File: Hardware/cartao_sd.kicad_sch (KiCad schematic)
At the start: 2 parts, among them J17 Micro_SD_Card, U11 74LVC125

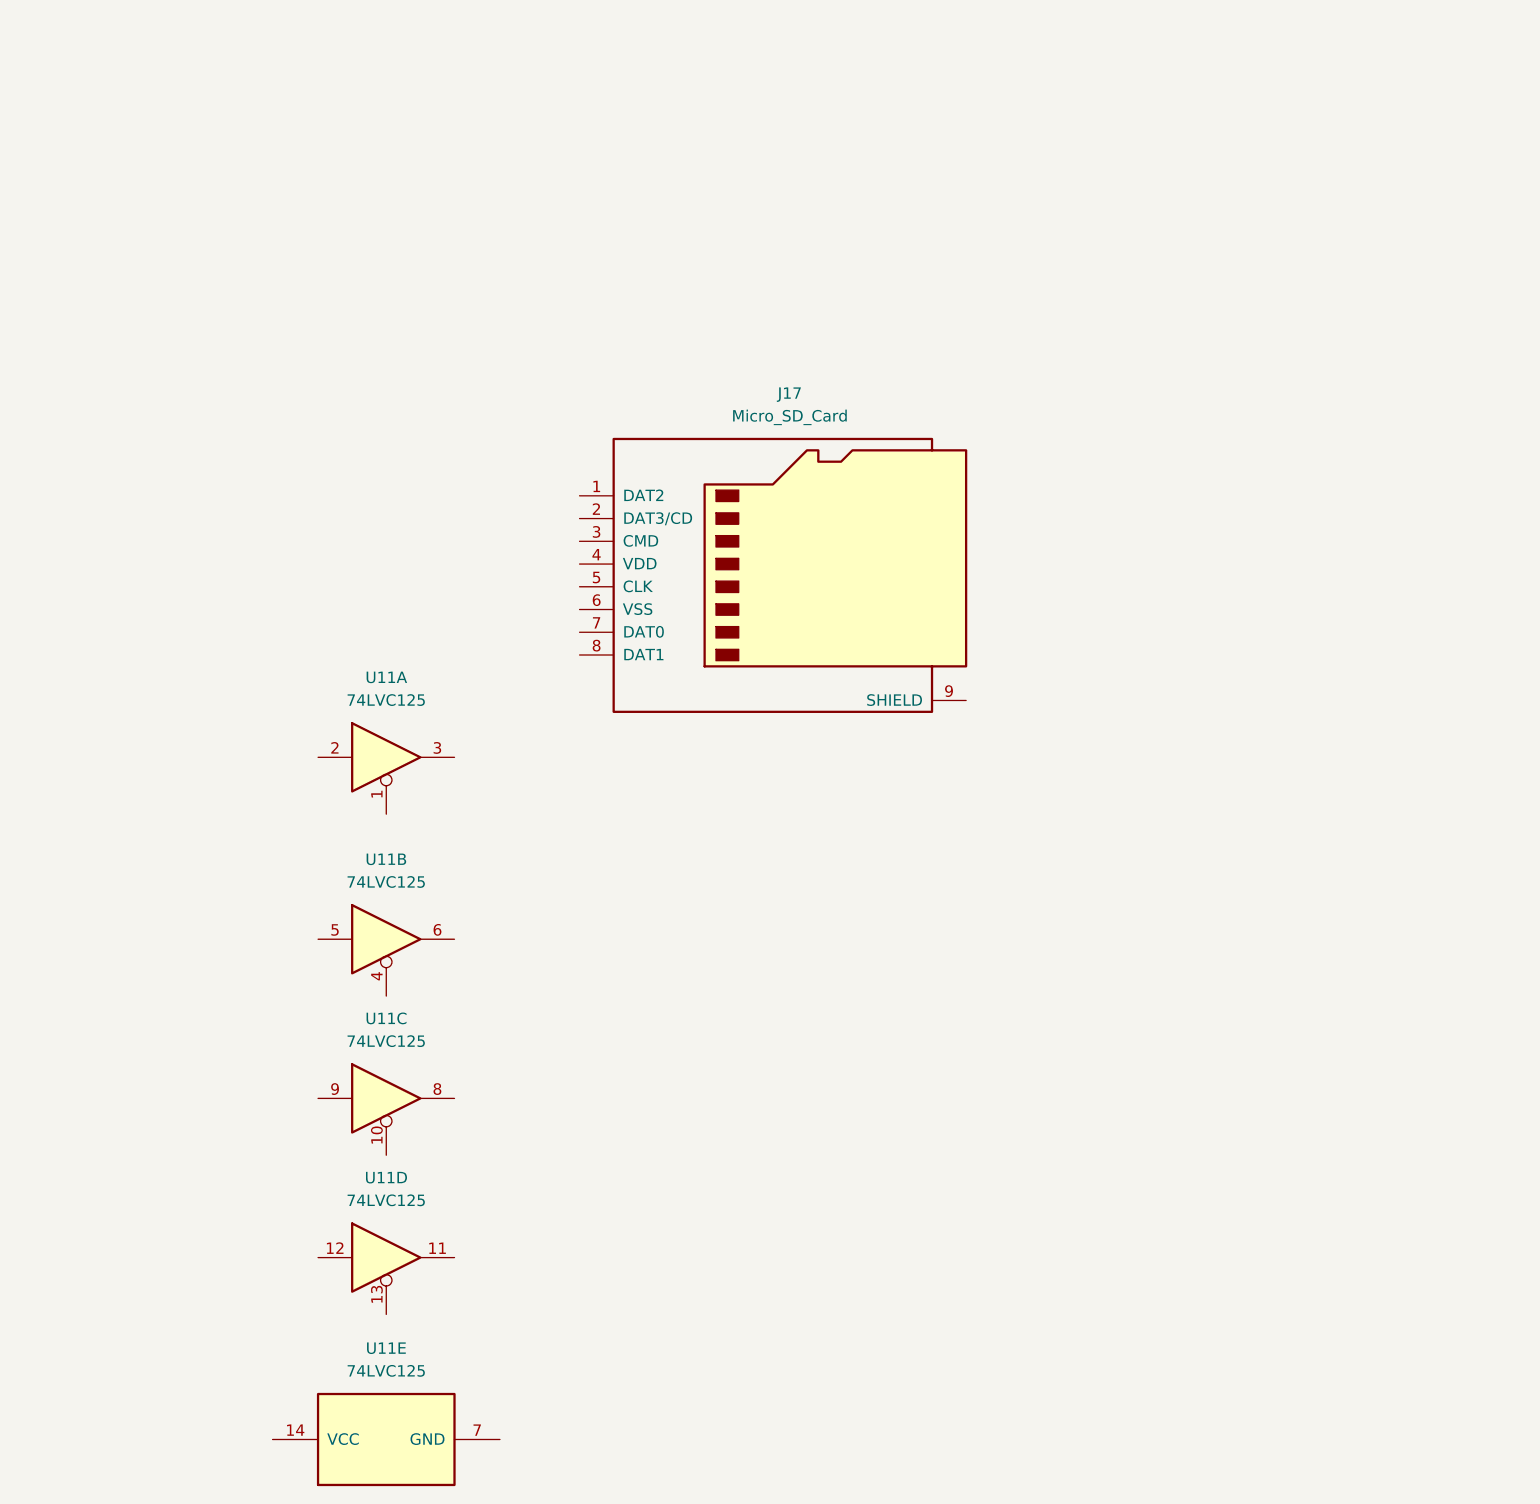
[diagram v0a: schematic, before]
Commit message: add circuito cartão sd
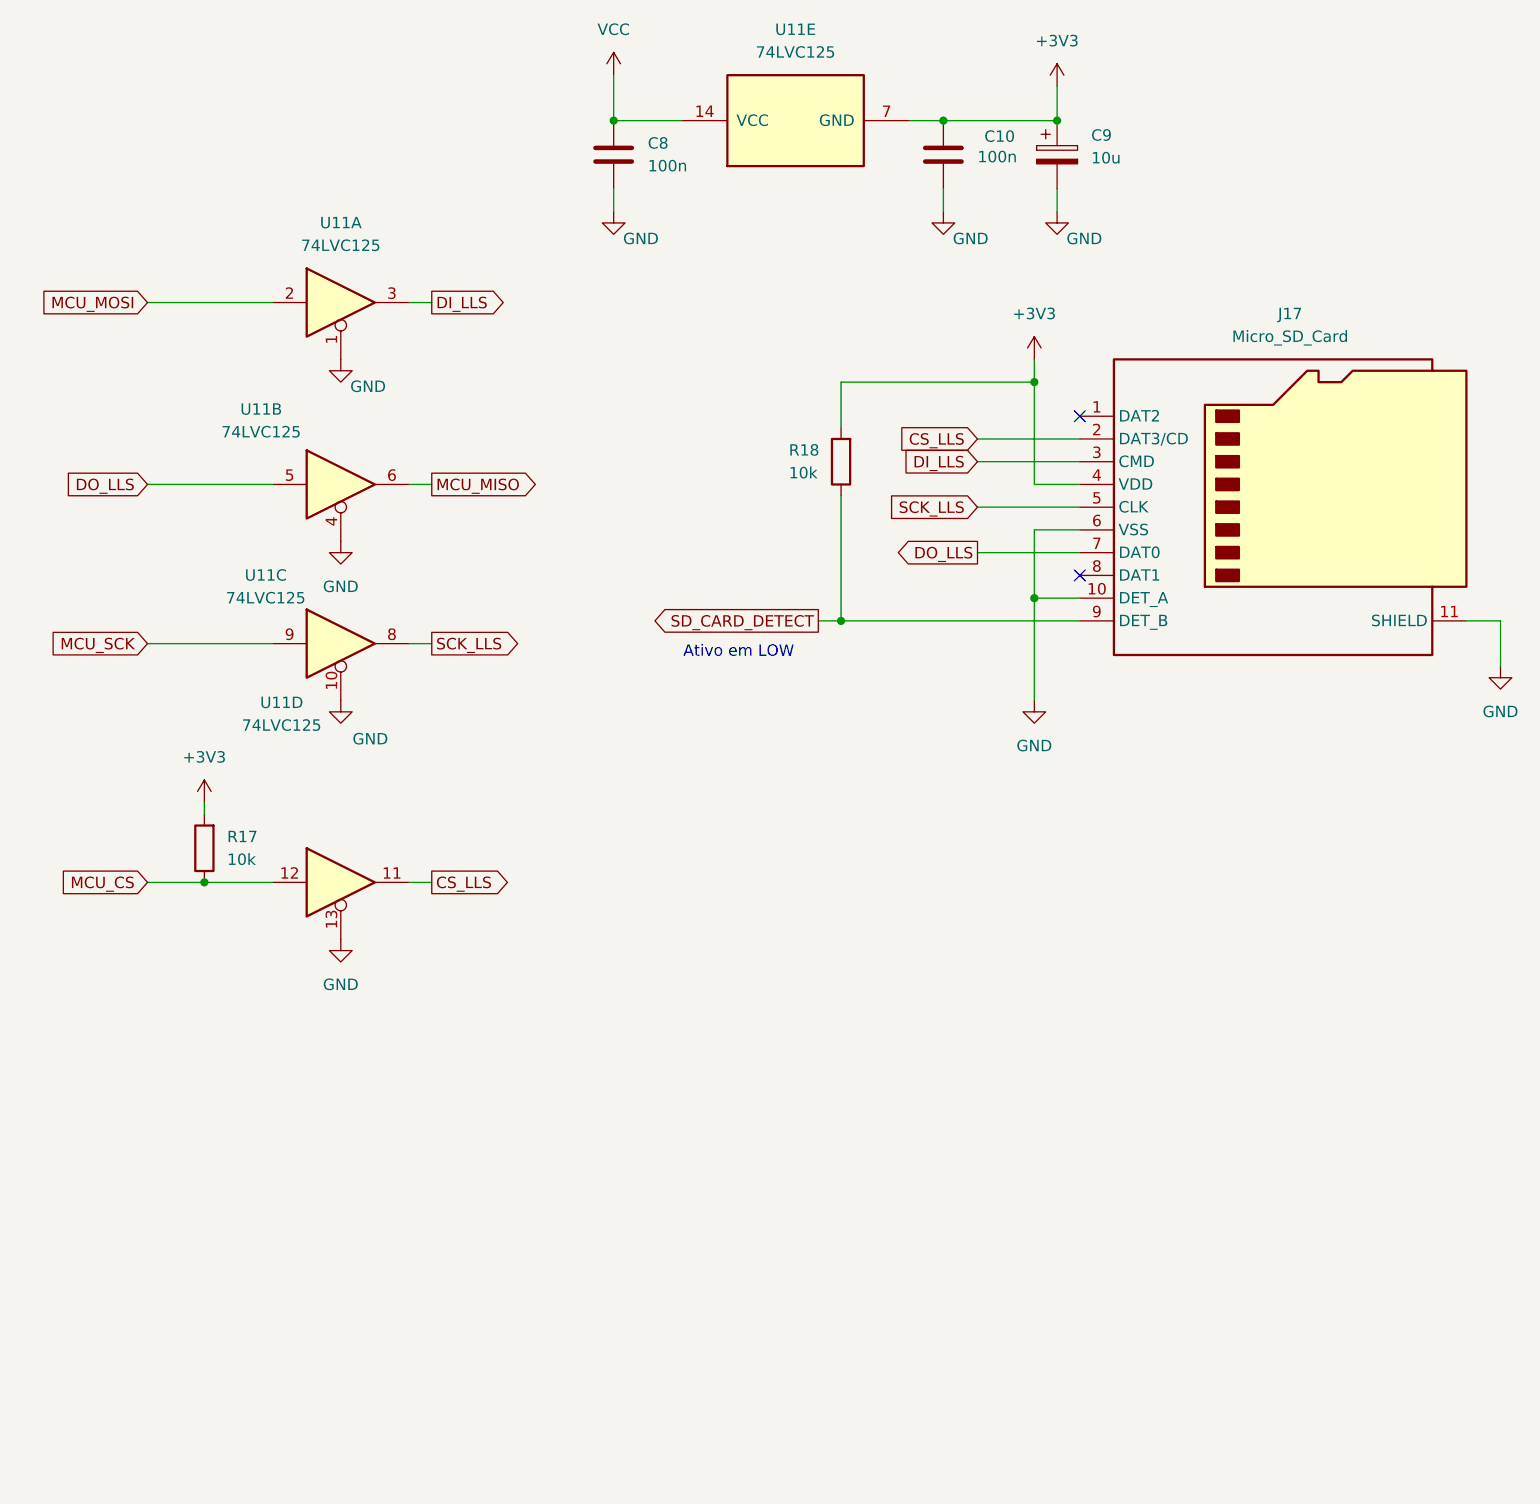
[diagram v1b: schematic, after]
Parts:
- added C10, C8: 100n, symbol Device:C
- added C9: 10u, symbol Device:C_Polarized
- added R17, R18: 10k, symbol Device:R
- J17: footprint Connector_Card:microSD_HC_Wuerth_693072010801 -> Connector_Card:microSD_HC_Molex_104031-0811; symbol Connector:Micro_SD_Card -> Connector:Micro_SD_Card_Det2
- U11: footprint Package_DIP:DIP-14_W7.62mm -> Package_SO:TSSOP-14_4.4x5mm_P0.65mm
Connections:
- net GND: now reaches U11.10
- net GND: now also J17.10 (DET_A), J17.11 (SHIELD), J17.6 (VSS), U11.1, U11.13, U11.4, C10.2, C8.2, C9.2
- net SCK_LLS: now reaches U11.8
- net SCK_LLS: now also J17.5 (CLK)
- net MCU_SCK: now reaches U11.9
- net CS_LLS: now reaches J17.2 (DAT3/CD)
- net CS_LLS: now also U11.11
- net DI_LLS: now reaches J17.3 (CMD)
- net DI_LLS: now also U11.3
- net +3V3: now reaches J17.4 (VDD)
- net +3V3: now also U11.7 (GND), C10.1, C9.1, R17.2, R18.2
- net DO_LLS: now reaches J17.7 (DAT0)
- net DO_LLS: now also U11.5
- net SD_CARD_DETECT: now reaches J17.9 (DET_B)
- net SD_CARD_DETECT: now also R18.1
- net VCC: now reaches U11.14 (VCC)
- net VCC: now also C8.1
- net MCU_MISO: now reaches U11.6
- net MCU_MOSI: now reaches U11.2
- net MCU_CS: now reaches U11.12
- net MCU_CS: now also R17.1
- no-connect marks 0 -> 2
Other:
- note added: "Ativo em LOW"
- moved on the sheet: U11A, U11B, U11C, U11D, U11E

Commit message: design sensores pronto
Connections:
- net MCU_CS renamed SD_CS
- net MCU_MISO renamed SD_MISO
- net MCU_SCK renamed SD_SCK
- net SD_CARD_DETECT renamed SD_CD
- net VCC renamed +5V
